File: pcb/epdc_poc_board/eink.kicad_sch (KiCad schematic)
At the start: 54 parts, among them J301 AXE550127, J302 FH26W-39S-0.3SHW, U301 LM358, U302 LT1945, U303 LT3471

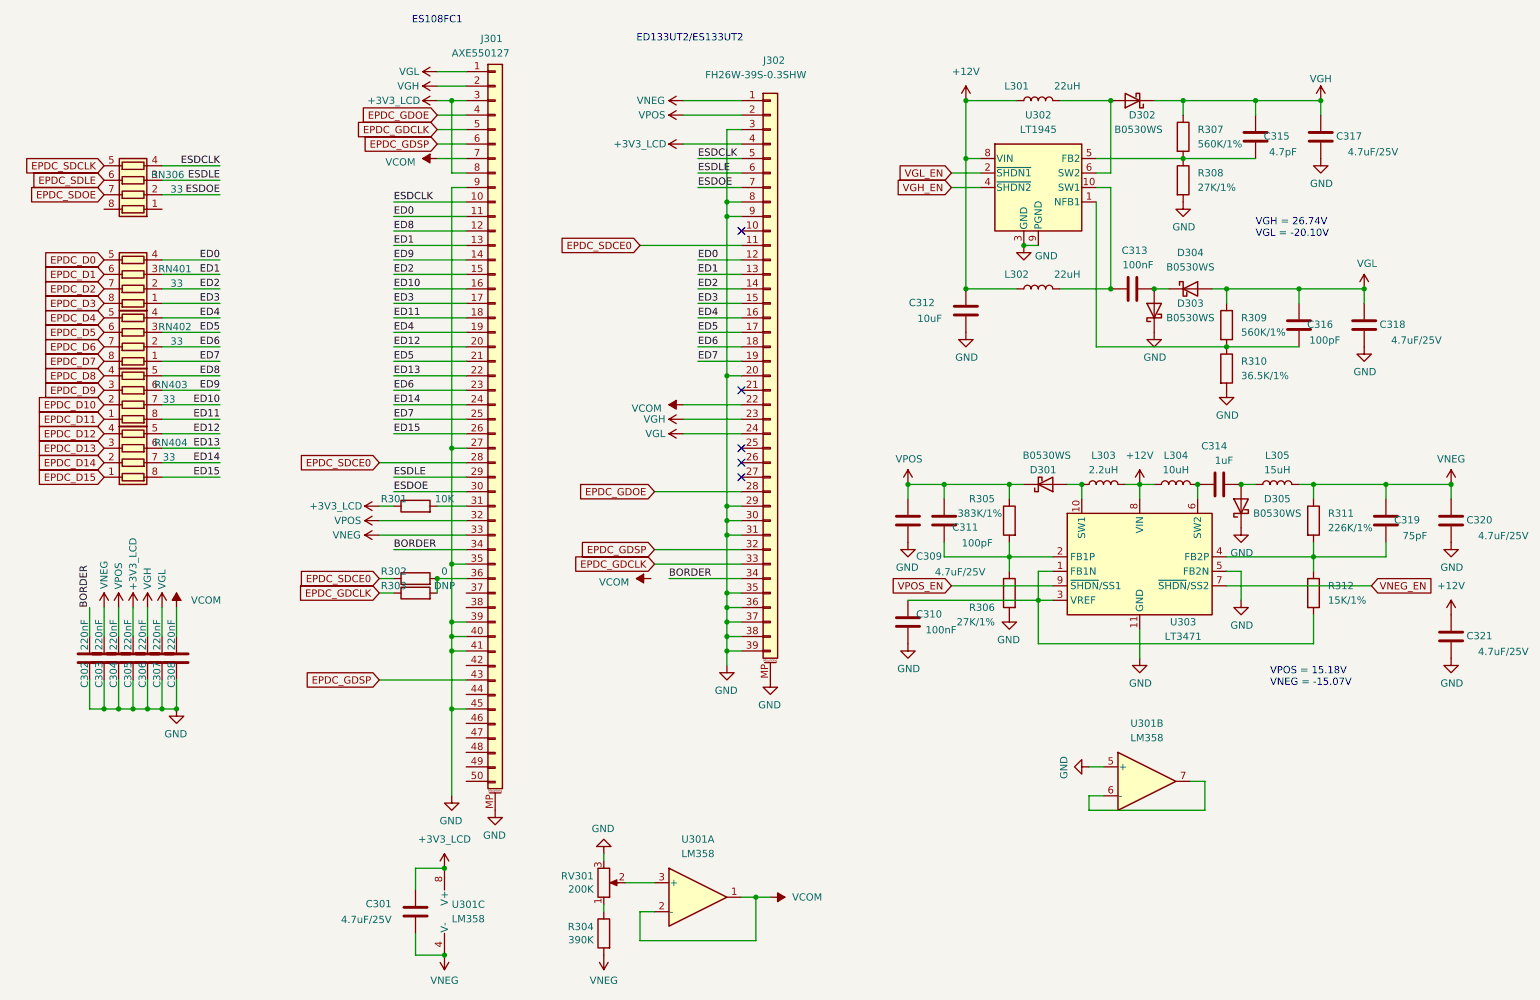
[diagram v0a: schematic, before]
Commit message: - wip epdc poc board, going to remove vga input
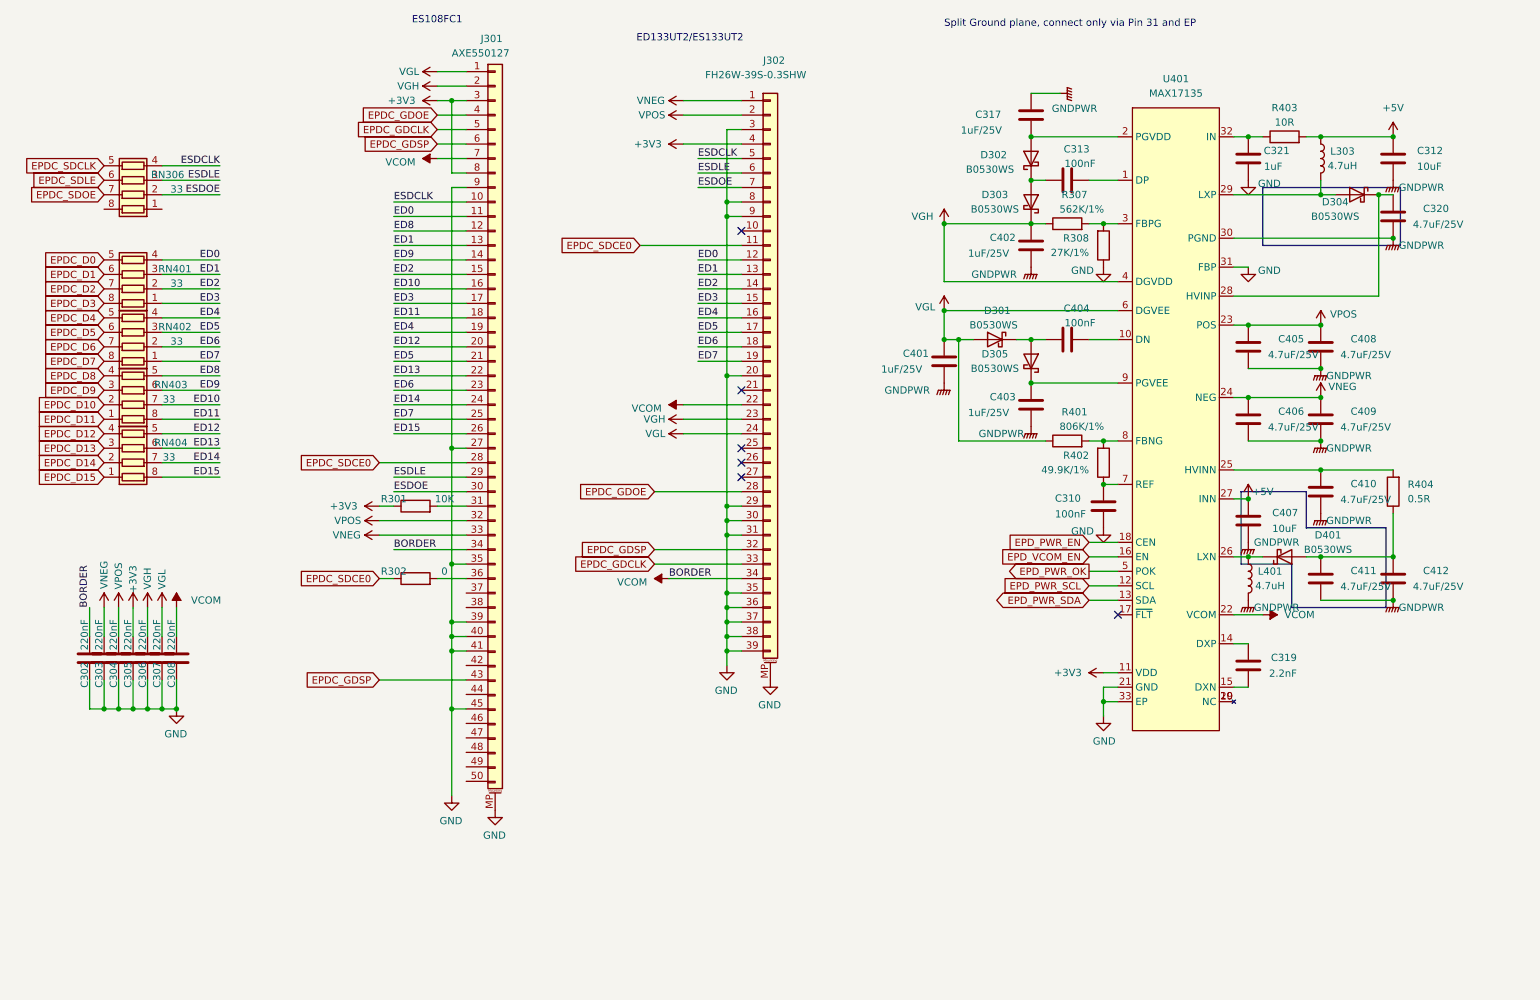
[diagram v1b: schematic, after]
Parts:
- removed C301, C309, C318: 4.7uF/25V, Capacitor_SMD:C_0805_2012Metric, symbol Device:C
- removed C311, C316: 100pF, Capacitor_SMD:C_0402_1005Metric, symbol Device:C
- removed C314: 1uF, Capacitor_SMD:C_0402_1005Metric, symbol Device:C
- removed C315: 4.7pF, Capacitor_SMD:C_0402_1005Metric, symbol Device:C
- removed L301, L302: 22uH, footprints:L_1212, symbol Device:L
- removed L304: 10uH, footprints:L_1212, symbol Device:L
- removed L305: 15uH, footprints:L_1212, symbol Device:L
- removed R303: DNP, Resistor_SMD:R_0402_1005Metric, symbol Device:R
- removed R304: 390K, Resistor_SMD:R_0402_1005Metric, symbol Device:R
- removed R305: 383K/1%, Resistor_SMD:R_0402_1005Metric, symbol Device:R
- removed R306: 27K/1%, Resistor_SMD:R_0402_1005Metric, symbol Device:R
- removed R309: 560K/1%, Resistor_SMD:R_0402_1005Metric, symbol Device:R
- removed R310: 36.5K/1%, Resistor_SMD:R_0402_1005Metric, symbol Device:R
- removed R311: 226K/1%, Resistor_SMD:R_0402_1005Metric, symbol Device:R
- removed R312: 15K/1%, Resistor_SMD:R_0402_1005Metric, symbol Device:R
- removed RV301: 200K, Potentiometer_SMD:Potentiometer_Vishay_TS53YL_Vertical, symbol Sitina-rescue:R_POT-Device
- removed U301: LM358, Package_SO:SO-8_3.9x4.9mm_P1.27mm, symbol Amplifier_Operational:LM358
- removed U302: LT1945, Package_SO:MSOP-10_3x3mm_P0.5mm, symbol Regulator_Switching:LT1945
- removed U303: LT3471, Package_DFN_QFN:DFN-10-1EP_3x3mm_P0.5mm_EP1.65x2.38mm, symbol Regulator_Switching:LT3471
- added C401, C402, C403: 1uF/25V, Capacitor_SMD:C_0805_2012Metric, symbol Device:C
- added C404: 100nF, Capacitor_SMD:C_0402_1005Metric, symbol Device:C
- added C405, C406, C408, C409, C410, C411, C412: 4.7uF/25V, Capacitor_SMD:C_0805_2012Metric, symbol Device:C
- added C407: 10uF, Capacitor_SMD:C_0603_1608Metric, symbol Device:C
- added D401: B0530WS, Diode_SMD:D_SOD-323, symbol Device:D_Schottky
- added L401: 4.7uH, footprints:L_1212, symbol Device:L
- added R401: 806K/1%, Resistor_SMD:R_0402_1005Metric, symbol Device:R
- added R402: 49.9K/1%, Resistor_SMD:R_0402_1005Metric, symbol Device:R
- added R403: 10R, Resistor_SMD:R_0402_1005Metric, symbol Device:R
- added R404: 0.5R, Resistor_SMD:R_0603_1608Metric, symbol Device:R
- added U401: MAX17135, Package_DFN_QFN:QFN-32-1EP_5x5mm_P0.5mm_EP3.1x3.1mm_ThermalVias, symbol symbols:MAX17135
- C317: value 4.7uF/25V -> 1uF/25V
- C319: value 75pF -> 2.2nF
- C321: value 4.7uF/25V -> 1uF
- L303: value 2.2uH -> 4.7uH
- R307: value 560K/1% -> 562K/1%
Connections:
- net BORDER is gone; now on net VCOM: C302.1, J301.34 (Pin_34), J302.34 (Pin_34)
- net GND: now also R308.1, U401.21 (GND), U401.31 (FBP), U401.33 (EP); no longer C312.1, C317.1, C320.1, D303.1 (K), D305.1 (K), R308.2
- net VCOM: now also U401.22 (VCOM)
- net VGH: now also D303.1 (K), C402.2, U401.4 (DGVDD); no longer C317.2, D302.1 (K)
- net VGL: now also D301.2 (A), C401.2, R401.1, U401.6 (DGVEE); no longer D304.2 (A)
- net VNEG: now also C406.2, C409.2, U401.24 (NEG); no longer C319.2, C320.2
- net VPOS: now also C405.2, C408.2, U401.23 (POS); no longer D301.1 (K)
- net at C310.2: now also R402.1, U401.7 (REF)
- net +5V: now reaches L303.1
- net +5V: now also C312.2, C407.2, R403.2, U401.27 (INN); no longer D301.2 (A)
- net at C319.1: now also U401.15 (DXN)
- net at D305.2 (A): now also D301.1 (K), C404.1
- net at C313.1: now also D302.1 (K), D303.2 (A)
- net at R307.2: now also R308.2, U401.3 (FBPG); no longer R308.1
- net at D302.2 (A): now also C317.1, U401.2 (PGVDD)
- removed net +12V: C312.2, C321.2, L303.2
- net +3V3_LCD renamed +3V3
- net +3V3: now also U401.11 (VDD)
- new net: D304.2 (A), L303.2, U401.29 (LXP)
- new net: C320.2, D304.1 (K), U401.28 (HVINP)
- new net: C411.2, C412.2, D401.2 (A), R404.1
- new net: C404.2, U401.10 (DN)
- new net: C313.2, U401.1 (DP)
- new net: C403.2, D305.1 (K), U401.9 (PGVEE)
- new net: R401.2, R402.2, U401.8 (FBNG)
- new net: C319.2, U401.14 (DXP)
- new net: U401.19 (NC), U401.20 (NC)
- new net: C410.2, R404.2, U401.25 (HVINN)
- new net: D401.1 (K), L401.1, U401.26 (LXN)
- new net: C321.2, R403.1, U401.32 (IN)
- new net EPD_PWR_EN: U401.18 (CEN)
- new net EPD_PWR_OK: U401.5 (POK)
- new net EPD_PWR_SCL: U401.12 (SCL)
- new net EPD_PWR_SDA: U401.13 (SDA)
- new net EPD_VCOM_EN: U401.16 (EN)
- new net GNDPWR: C312.1, C317.2, C320.1, C401.1, C402.1, C403.1, C405.1, C406.1, C407.1, C408.1, C409.1, C410.1, C411.1, C412.1, L401.2, U401.30 (PGND)
- no-connect marks 5 -> 6
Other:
- note added: "Split Ground plane, connect only via Pin 31 and EP"
- note removed: "VGH = 26.74V VGL = -20.10V"
- note removed: "VPOS = 15.18V VNEG = -15.07V"
- moved on the sheet: C310, C312, C313, C317, C319, C320, C321, D301, D302, D303, D304, D305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

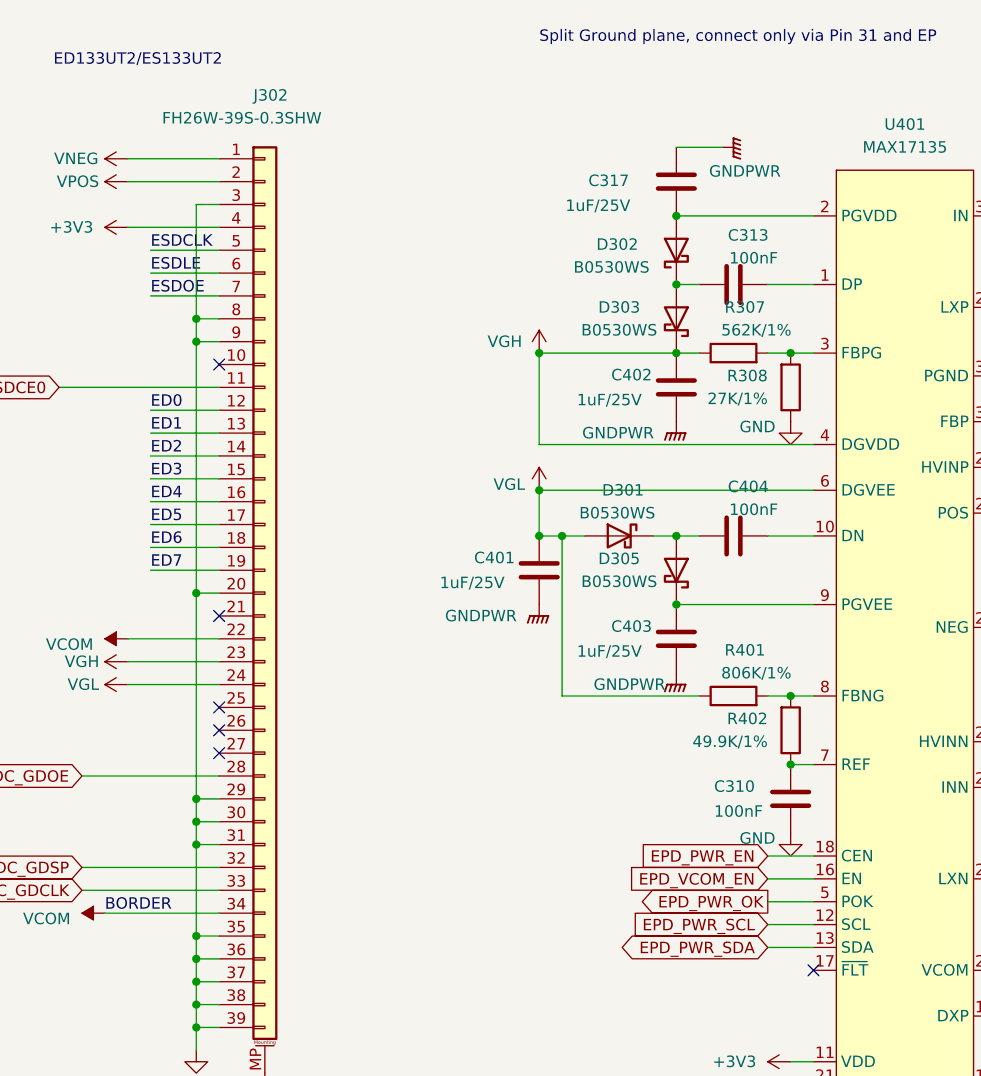
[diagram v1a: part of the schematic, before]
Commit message: pcb: switch to s6 for epdc board
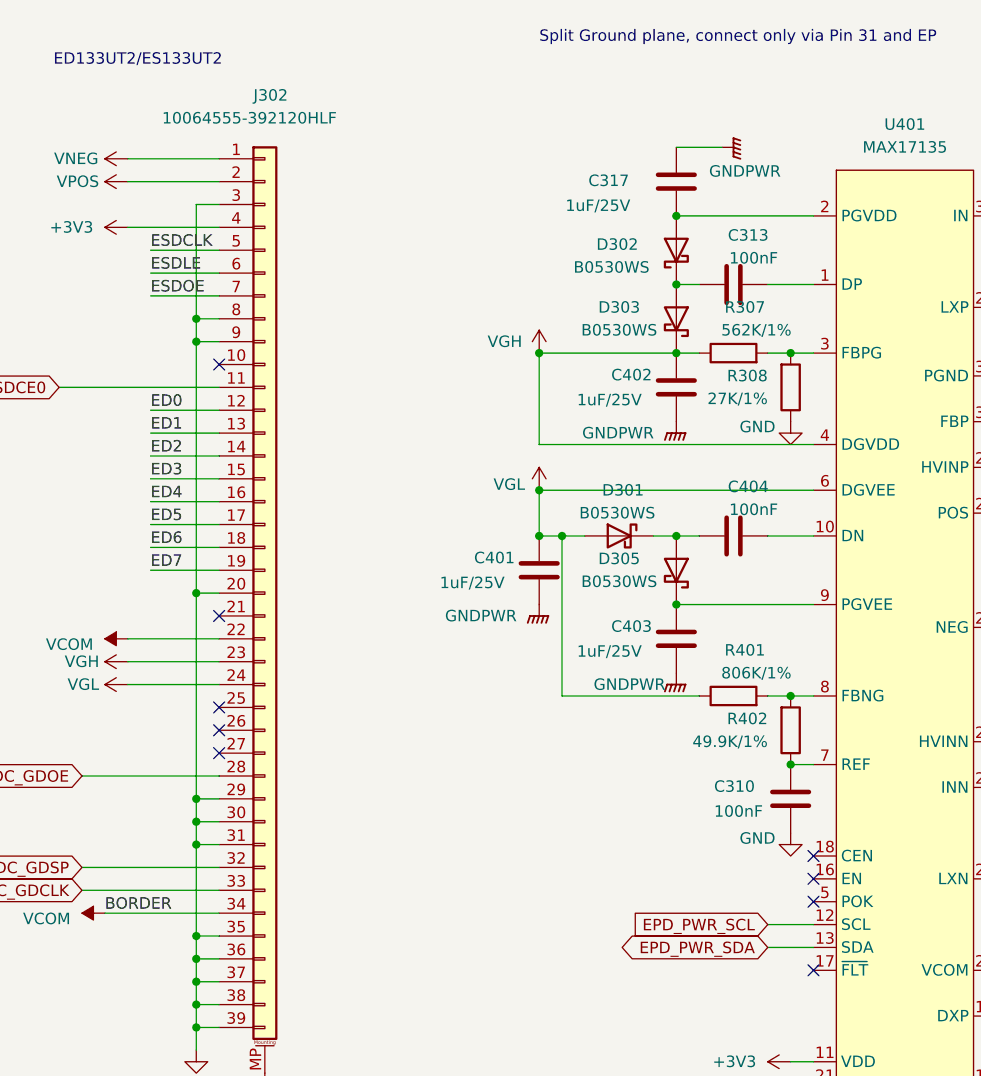
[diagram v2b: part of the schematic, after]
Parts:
- J302: value FH26W-39S-0.3SHW -> 10064555-392120HLF; footprint footprints:HRS_FH26W-39S-0.3SHW(60) -> footprints:FCI_10064555-392120HLF
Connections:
- net EPD_PWR_EN: no longer names the net of U401.18 (CEN)
- net EPD_PWR_OK: no longer names the net of U401.5 (POK)
- net EPD_VCOM_EN: no longer names the net of U401.16 (EN)
- no-connect marks 6 -> 9
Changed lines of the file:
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@@
   (no_connect (at 143.51 97.79))
   (no_connect (at 143.51 100.33))
+  (no_connect (at 209.55 111.76))
+  (no_connect (at 209.55 114.3))
+  (no_connect (at 209.55 116.84))
   (no_connect (at 209.55 124.46))
   (wire (pts (xy 29.21 123.19) (xy 29.21 128.27))
@@
     (stroke (width 0) (type default) (color 0 0 0 0))
   )
-  (wire (pts (xy 204.47 111.76) (xy 209.55 111.76))
-    (stroke (width 0) (type default) (color 0 0 0 0))
-  )
-  (wire (pts (xy 204.47 114.3) (xy 209.55 114.3))
-    (stroke (width 0) (type default) (color 0 0 0 0))
-  )
-  (wire (pts (xy 204.47 116.84) (xy 209.55 116.84))
-    (stroke (width 0) (type default) (color 0 0 0 0))
-  )
   (wire (pts (xy 204.47 119.38) (xy 209.55 119.38))
     (stroke (width 0) (type default) (color 0 0 0 0))
@@
     (effects (font (size 1.27 1.27)) (justify right))
     (property "Intersheet References" "${INTERSHEET_REFS}" (id 0) (at 113.8221 115.4906 0)
-      (effects (font (size 1.27 1.27)) (justify right) hide)
-    )
-  )
-  (global_label "EPD_PWR_EN" (shape input) (at 204.47 111.76 180) (fields_autoplaced)
-    (effects (font (size 1.27 1.27)) (justify right))
-    (property "Intersheet References" "${INTERSHEET_REFS}" (id 0) (at 190.057 111.6806 0)
-      (effects (font (size 1.27 1.27)) (justify right) hide)
-    )
-  )
-  (global_label "EPD_VCOM_EN" (shape input) (at 204.47 114.3 180) (fields_autoplaced)
-    (effects (font (size 1.27 1.27)) (justify right))
-    (property "Intersheet References" "${INTERSHEET_REFS}" (id 0) (at 188.9079 114.2206 0)
-      (effects (font (size 1.27 1.27)) (justify right) hide)
-    )
-  )
-  (global_label "EPD_PWR_OK" (shape output) (at 204.47 116.84 180) (fields_autoplaced)
-    (effects (font (size 1.27 1.27)) (justify right))
-    (property "Intersheet References" "${INTERSHEET_REFS}" (id 0) (at 189.936 116.7606 0)
       (effects (font (size 1.27 1.27)) (justify right) hide)
     )
@@
       (effects (font (size 1.27 1.27)) (justify left))
     )
-    (property "Value" "FH26W-39S-0.3SHW" (id 1) (at 137.16 29.7814 0)
-      (effects (font (size 1.27 1.27)) (justify left))
-    )
-    (property "Footprint" "footprints:HRS_FH26W-39S-0.3SHW(60)" (id 2) (at 148.59 82.55 0)
-      (effects (font (size 1.27 1.27)) hide)
-    )
+    (property "Value" "10064555-392120HLF" (id 1) (at 137.16 29.7814 0)
+      (effects (font (size 1.27 1.27)) (justify left))
+    )
+    (property "Footprint" "footprints:FCI_10064555-392120HLF" (id 2) (at 148.59 82.55 0)
+      (effects (font (size 1.27 1.27)) hide)
+    )

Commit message: pcb: mb r0.1, caster r0.1 freeze
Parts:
- C302, C303, C304, C305, C306, C307, C308: LCSC (none) -> C880414; Ref.Price (none) -> 0.0036
- C310, C313, C404: LCSC (none) -> C56392; Ref.Price (none) -> 0.0023
- C312, C407: LCSC (none) -> C105490; Ref.Price (none) -> 0.0165
- C317, C401, C402, C403: LCSC (none) -> C111769; Ref.Price (none) -> 0.0174
- C319: LCSC (none) -> C913886; Ref.Price (none) -> 0.0024
- C320, C405, C406, C408, C409, C410, C411, C412: LCSC (none) -> C105489; Ref.Price (none) -> 0.0271
- C321: footprint Capacitor_SMD:C_0805_2012Metric -> Capacitor_SMD:C_0402_1005Metric; LCSC (none) -> C157353; Ref.Price (none) -> 0.0034
- D301, D302, D303, D304, D305, D401: LCSC (none) -> C475612; Ref.Price (none) -> 0.0209
- J301: LCSC (none) -> -; Ref.Price (none) -> 0
- J302: LCSC (none) -> 609-10064555-392120HLFCT-ND; Ref.Price (none) -> 0.95
- L303, L401: LCSC (none) -> C340379; Ref.Price (none) -> 0.0643
- R301: value 10K -> 4.7K; LCSC (none) -> C105870; Ref.Price (none) -> 0.0006
- R302: value 0 -> 0R; LCSC (none) -> C60485; Ref.Price (none) -> 0.008
- R307: LCSC (none) -> C273337; Ref.Price (none) -> 0.001
- R308: LCSC (none) -> C138022; Ref.Price (none) -> 0.0029
- R401: LCSC (none) -> C375495; Ref.Price (none) -> 0.0008
- R402: LCSC (none) -> C137969; Ref.Price (none) -> 0.001
- R403: LCSC (none) -> C137925; Ref.Price (none) -> 0.0006
- R404: LCSC (none) -> C45312; Ref.Price (none) -> 0.004
- RN306, RN401, RN402, RN403, RN404: value 33 -> 33R; LCSC (none) -> C148513; Ref.Price (none) -> 0.0168
- U401: Ref.Price (none) -> 3.61
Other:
- company: (none) -> Copyright 2021 Modos / Engineer: Wenting Zhang
- title: (none) -> Caster EPDC
